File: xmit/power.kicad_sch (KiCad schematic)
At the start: 18 parts, among them U1 74LVC1G66, U10 L7812, U12 74LVC1G66, U13 74LVC1G66, U2 74LVC1G66, U3 74LVC1G66, U4 74LVC1G66, U5 74LVC1G66, U6 74LVC1G66, U7 TPS7A20xxxDBV, U9 TLV760

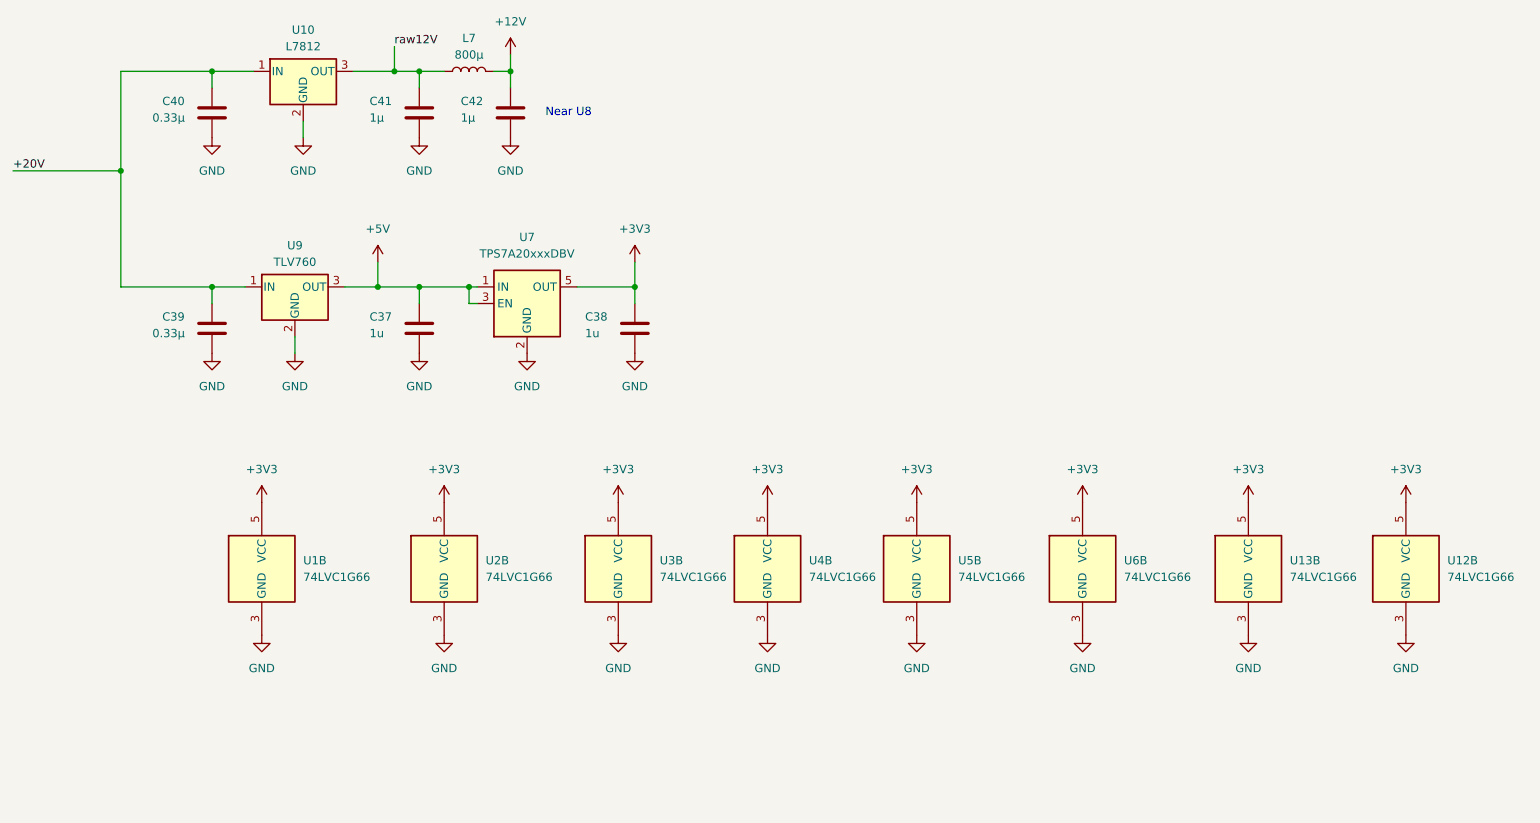
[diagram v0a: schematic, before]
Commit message: More layout cleanup.
This is a checkpoint before I move all of the power management to a separate board. Next step is to move all power management to a separate board.
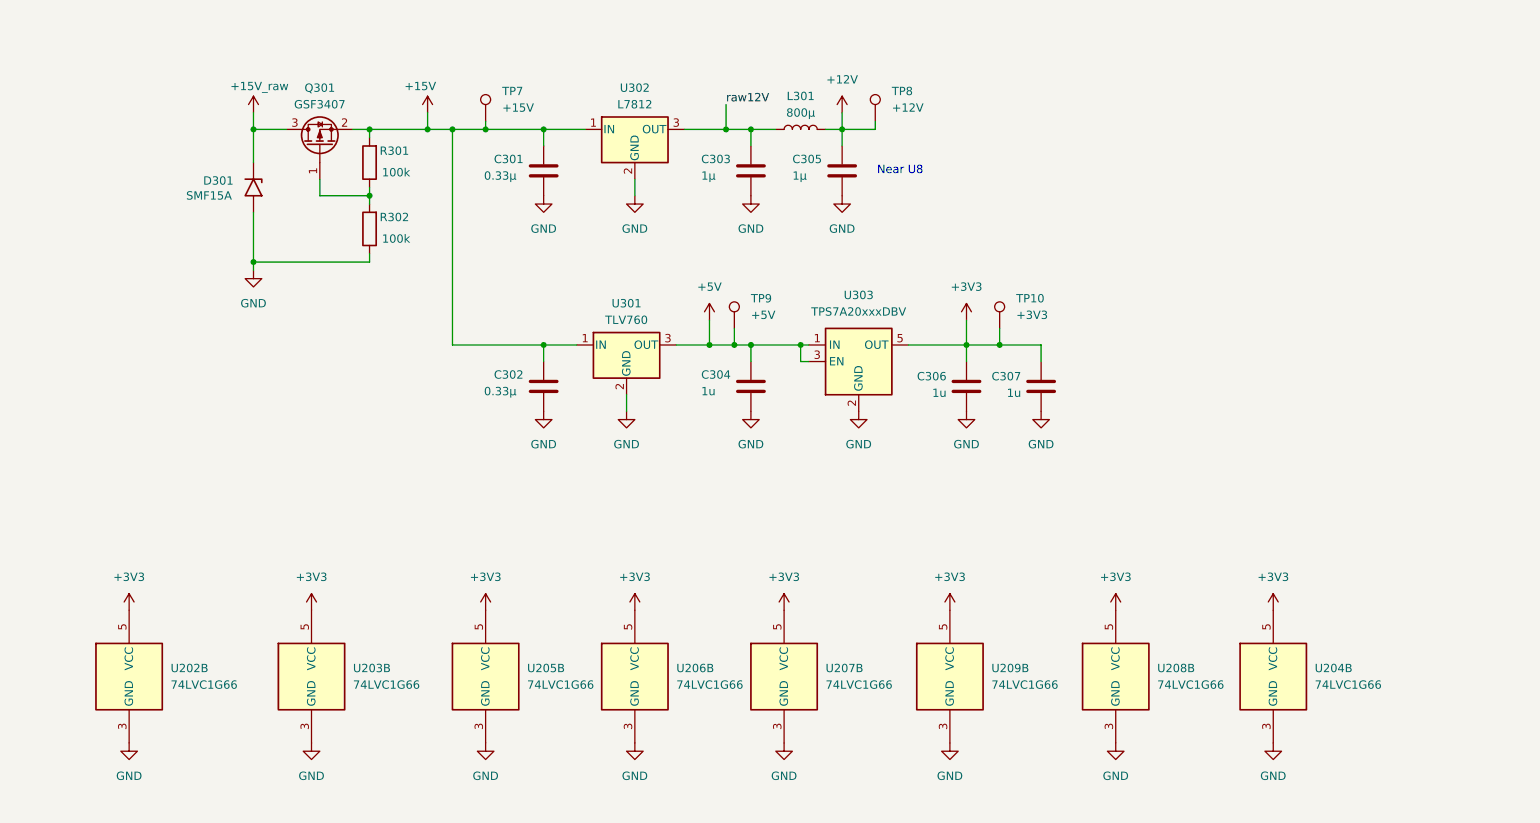
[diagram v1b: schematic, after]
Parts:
- added C307: 1u, Capacitor_SMD:C_0805_2012Metric, symbol Device:C
- added D301: SMF15A, Diode_SMD:D_SMF, symbol Diode:SMF5V0A
- added Q301: GSF3407, Package_TO_SOT_SMD:SOT-23, symbol Transistor_FET:DMP3099L
- added R301, R302: 100k, Resistor_SMD:R_0805_2012Metric_Pad1.20x1.40mm_HandSolder, symbol Device:R
- added TP10: +3V3, TestPoint:TestPoint_Pad_1.0x1.0mm, symbol Connector:TestPoint
- added TP7: +15V, TestPoint:TestPoint_Pad_1.0x1.0mm, symbol Connector:TestPoint
- added TP8: +12V, TestPoint:TestPoint_Pad_1.0x1.0mm, symbol Connector:TestPoint
- added TP9: +5V, TestPoint:TestPoint_Pad_1.0x1.0mm, symbol Connector:TestPoint
- renumbered C40 to C301, C39 to C302, C41 to C303, C37 to C304, C42 to C305, C38 to C306, L7 to L301, U1 to U202, U2 to U203, U12 to U204, U3 to U205, U4 to U206, U5 to U207, U13 to U208, U6 to U209, U9 to U301, U10 to U302, U7 to U303
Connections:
- net +12V: now also TP8.1
- net +3V3: now also C307.2, TP10.1
- net +5V: now also TP9.1
- net GND: now also C307.1, D301.2 (A2), R302.1
- net +20V renamed +15V
- net +15V: now also Q301.2 (S), R301.2, TP7.1
- new net: Q301.1 (G), R301.1, R302.2
- new net +15V_raw: D301.1 (A1), Q301.3 (D)
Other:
- moved on the sheet: C301, C302, C303, C304, C305, C306, L301, U202B, U203B, U204B, U205B, U206B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

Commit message: changes up to first spin
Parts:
- removed C301: 0.33µ, Capacitor_SMD:C_0805_2012Metric, symbol Device:C
- removed D301: SMF15A, Diode_SMD:D_SMF, symbol Diode:SMF5V0A
- removed TP10: +3V3, TestPoint:TestPoint_Pad_1.0x1.0mm, symbol Connector:TestPoint
- removed TP7: +15V, TestPoint:TestPoint_Pad_1.0x1.0mm, symbol Connector:TestPoint
- removed TP8: +12V, TestPoint:TestPoint_Pad_1.0x1.0mm, symbol Connector:TestPoint
- removed TP9: +5V, TestPoint:TestPoint_Pad_1.0x1.0mm, symbol Connector:TestPoint
- removed U301: TLV760, Package_TO_SOT_SMD:TSOT-23, symbol Regulator_Linear:L7805
- removed U302: L7812, Package_TO_SOT_THT:TO-220-3_Horizontal_TabDown, symbol Regulator_Linear:L7812
- added D301, D302: LED, LED_SMD:LED_0603_1608Metric, symbol Device:LED
- added L302: 1µH, Inductor_SMD:L_0805_2012Metric_Pad1.05x1.20mm_HandSolder, symbol Device:L
- added Q302: AO3407A, Package_TO_SOT_SMD:SOT-23, symbol Transistor_FET:DMP3099L
- added R303, R304: 200k, Resistor_SMD:R_0805_2012Metric_Pad1.20x1.40mm_HandSolder, symbol Device:R
- added R305: 2.2k, Resistor_SMD:R_0603_1608Metric, symbol Device:R
- added R306: 100, Resistor_SMD:R_0603_1608Metric, symbol Device:R
- C301: renamed from C303; KiLib_Generator (none) -> SMD_2terminal_chip_molded; LCSC Part # (none) -> C76645; now left out of the parts list
- C302: value 0.33µ -> 1µ; KiLib_Generator (none) -> SMD_2terminal_chip_molded; LCSC Part # (none) -> C76645; now left out of the parts list
- C303: renamed from C305; KiLib_Generator (none) -> SMD_2terminal_chip_molded; LCSC Part # (none) -> C76645; now left out of the parts list
- C304: value 1u -> 1µ; KiLib_Generator (none) -> SMD_2terminal_chip_molded; LCSC Part # (none) -> C76645; now left out of the parts list
- C305: renamed from C306; value 1u -> 1µ; KiLib_Generator (none) -> SMD_2terminal_chip_molded; LCSC Part # (none) -> C76645; now left out of the parts list
- C306: renamed from C307; value 1u -> 1µ; KiLib_Generator (none) -> SMD_2terminal_chip_molded; LCSC Part # (none) -> C76645; now left out of the parts list
- L301: value 800µ -> 1µH; KiLib_Generator (none) -> SMD_2terminal_chip_molded; LCSC Part # (none) -> C19533; now left out of the parts list
- Q301: value GSF3407 -> AO3407A; KiLib_Generator (none) -> package/gullwing; LCSC Part # (none) -> C15155; now left out of the parts list
- R301, R302: value 100k -> 200k; KiLib_Generator (none) -> SMD_2terminal_chip_molded; LCSC Part # (none) -> C17539; now left out of the parts list
- U202, U203, U204, U205, U206, U207, U208, U209: footprint Package_TO_SOT_SMD:SOT-23-5_HandSoldering -> Package_TO_SOT_SMD:SOT-23-5; KiLib_Generator (none) -> package/gullwing; LCSC Part # (none) -> C113518
- U301: renamed from U303; value TPS7A20xxxDBV -> TPS7A2033PDBV; KiLib_Generator (none) -> package/gullwing; LCSC Part # (none) -> C7827; now left out of the parts list
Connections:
- net +12V is gone; now on net +15V: C303.2, L301.2
- net +15V: now also R305.1; no longer C302.2, Q301.2 (S), R301.2
- net +3V3: now also R306.1
- net +5V: now also L302.2
- net GND: now also D301.1 (K), D302.1 (K), R304.1
- net raw12V renamed +15V_safe
- net +15V_safe: now also Q301.2 (S), R301.2
- new net: Q302.1 (G), R303.1, R304.2
- new net: D301.2 (A), R305.2
- new net: D302.2 (A), R306.2
- new net +5V_raw: Q302.3 (D)
- new net +5V_safe: C302.2, L302.1, Q302.2 (S), R303.2
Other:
- moved on the sheet: C301, C303, C304, C305, C306, L301, U202B, U203B, U204B, U205B, U206B, U207B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
